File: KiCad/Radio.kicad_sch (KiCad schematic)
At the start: 2 parts, among them U3 RFM95W-868S2

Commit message: adjustments to work with JLC and to match with example
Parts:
- added C24: 1uF, Capacitor_SMD:C_0402_1005Metric, symbol Device:C_Small
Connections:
- net +3V3: now also C24.1
- net GND: now also C24.2
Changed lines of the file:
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@@
+		(color 0 0 0 0)
+	)
+	(junction
+		(at 133.35 68.58)
+		(diameter 0)
 		(color 0 0 0 0)
 	)
@@
 	(wire
 		(pts
-			(xy 133.35 67.31) (xy 133.35 78.74)
+			(xy 133.35 67.31) (xy 133.35 68.58)
 		)
 		(stroke
@@
 	(wire
 		(pts
+			(xy 120.65 68.58) (xy 133.35 68.58)
+		)
+		(stroke
+			(width 0)
+			(type default)
+		)
+	)
+	(wire
+		(pts
 			(xy 130.81 109.22) (xy 133.35 109.22)
 		)
@@
 	(wire
 		(pts
+			(xy 133.35 68.58) (xy 133.35 78.74)
+		)
+		(stroke
+			(width 0)
+			(type default)
+		)
+	)
+	(wire
+		(pts
 			(xy 152.4 101.6) (xy 146.05 101.6)
 		)
@@
 		(pts
 			(xy 113.03 88.9) (xy 120.65 88.9)
+		)
+		(stroke
+			(width 0)
+			(type default)
+		)
+	)
+	(wire
+		(pts
+			(xy 120.65 69.85) (xy 120.65 68.58)
 		)
 		(stroke
@@
 	(symbol
 		(lib_id "power:GND")
+		(at 120.65 74.93 0)
+		(unit 1)
+		(exclude_from_sim no)
+		(in_bom yes)
+		(on_board yes)
+		(dnp no)
+		(fields_autoplaced yes)
+		(property "Reference" "#PWR079"
+			(at 120.65 81.28 0)
+			(effects
+				(font
+					(size 1.27 1.27)
+				)
+				(hide yes)
+			)
+		)
+		(property "Value" "GND"
+			(at 120.65 80.01 0)
+			(effects
+				(font
+					(size 1.27 1.27)
+				)
+			)
+		)
+		(property "Footprint" ""
+			(at 120.65 74.93 0)
+			(effects
+				(font
+					(size 1.27 1.27)
+				)
+				(hide yes)
+			)
+		)
+		(property "Datasheet" ""
+			(at 120.65 74.93 0)
+			(effects
+				(font
+					(size 1.27 1.27)
+				)
+				(hide yes)
+			)
+		)
+		(property "Description" "Power symbol creates a global label with name \"GND\" , ground"
+			(at 120.65 74.93 0)
+			(effects
+				(font
+					(size 1.27 1.27)
+				)
+				(hide yes)
+			)
+		)
+		(pin "1"
+		)
+		(instances
+			(project ""
+				(path "/16f8cce7-467e-4342-b55a-00af81cd6f69/1c8bf498-9754-4bec-a707-8e930cfc3fe5"
+					(reference "#PWR079")
+					(unit 1)
+				)
+			)
+		)
+	)
+	(symbol
+		(lib_id "power:GND")
 		(at 147.32 86.36 0)
 		(unit 1)
@@
 					(unit 1)
 				)
+			)
+		)
+	)
+	(symbol
+		(lib_id "Device:C_Small")
+		(at 120.65 72.39 0)
+		(unit 1)
+		(exclude_from_sim no)
+		(in_bom yes)
+		(on_board yes)
+		(dnp no)
+		(fields_autoplaced yes)
+		(property "Reference" "C24"
+			(at 123.19 71.1262 0)
+			(effects
+				(font
+					(size 1.27 1.27)
+				)
+				(justify left)
+			)
+		)
+		(property "Value" "1uF"
+			(at 123.19 73.6662 0)
+			(effects
+				(font
+					(size 1.27 1.27)
+				)
+				(justify left)
+			)
+		)
+		(property "Footprint" "Capacitor_SMD:C_0402_1005Metric"
+			(at 120.65 72.39 0)
+			(effects
+				(font
+					(size 1.27 1.27)
+				)
+				(hide yes)
+			)
+		)
+		(property "Datasheet" "~"
+			(at 120.65 72.39 0)
+			(effects
+				(font
+					(size 1.27 1.27)
+				)
+				(hide yes)
+			)
+		)
+		(property "Description" "Unpolarized capacitor, small symbol"
+			(at 120.65 72.39 0)
+			(effects
+				(font
+					(size 1.27 1.27)
+				)
+				(hide yes)
+			)
+		)
+		(property "LCSC" "C52923"
+			(at 120.65 72.39 0)
+			(effects
+				(font
+					(size 1.27 1.27)
+				)
+			)
+		)
+		(pin "1"
+		)
+		(pin "2"
+		)
+		(instances
+			(project ""
+				(path "/16f8cce7-467e-4342-b55a-00af81cd6f69/1c8bf498-9754-4bec-a707-8e930cfc3fe5"
+					(reference "C24")
+					(unit 1)
+				)

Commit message: prepare to move barometer to front
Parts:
- AE2: now not fitted
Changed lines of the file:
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@@
 		(in_bom yes)
 		(on_board yes)
-		(dnp no)
+		(dnp yes)
 		(fields_autoplaced yes)
 		(property "Reference" "AE2"

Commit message: finalize board
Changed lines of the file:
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@@
 	(wire
 		(pts
-			(xy 118.11 96.52) (xy 120.65 96.52)
+			(xy 113.03 96.52) (xy 120.65 96.52)
 		)
 		(stroke
@@
 	(wire
 		(pts
-			(xy 147.32 86.36) (xy 149.86 86.36)
-		)
-		(stroke
-			(width 0)
-			(type default)
-		)
-	)
-	(wire
-		(pts
 			(xy 130.81 106.68) (xy 130.81 109.22)
 		)
@@
 	(hierarchical_label "RST"
 		(shape input)
-		(at 118.11 96.52 180)
+		(at 113.03 96.52 180)
 		(effects
 			(font
@@
 	(symbol
 		(lib_id "power:GND")
-		(at 147.32 86.36 0)
+		(at 149.86 86.36 0)
 		(unit 1)
 		(exclude_from_sim no)
@@
 		(fields_autoplaced yes)
 		(property "Reference" "#PWR043"
-			(at 147.32 92.71 0)
+			(at 149.86 92.71 0)
 			(effects
 				(font
@@
 		)
 		(property "Value" "GND"
-			(at 147.32 91.44 0)
+			(at 149.86 91.44 0)
 			(effects
 				(font
@@
 		)
 		(property "Footprint" ""
-			(at 147.32 86.36 0)
+			(at 149.86 86.36 0)
 			(effects
 				(font
@@
 		)
 		(property "Datasheet" ""
-			(at 147.32 86.36 0)
+			(at 149.86 86.36 0)
 			(effects
 				(font
@@
 		)
 		(property "Description" "Power symbol creates a global label with name \"GND\" , ground"
-			(at 147.32 86.36 0)
-			(effects
-				(font
+			(at 149.86 86.36 0)
+			(effects
+				(font

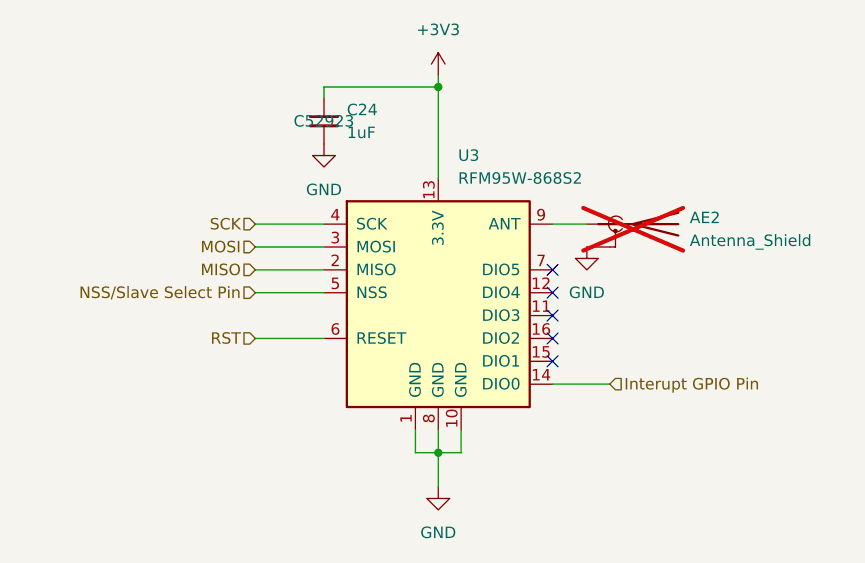
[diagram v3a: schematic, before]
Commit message: switch to BMI088 for IMU
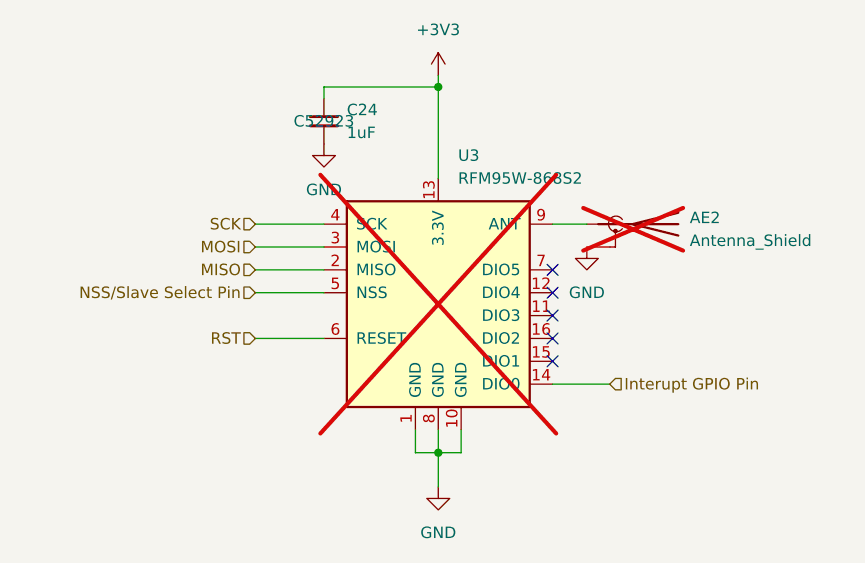
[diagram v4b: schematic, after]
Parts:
- U3: now not fitted
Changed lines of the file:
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@@
 		(in_bom yes)
 		(on_board yes)
-		(dnp no)
+		(dnp yes)
 		(property "Reference" "U3"
 			(at 135.5441 76.2 0)
